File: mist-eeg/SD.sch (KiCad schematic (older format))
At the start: 24 parts, among them J4 Micro_SD_Card_Det, Q2 NMOS_DGS (3.3V), Q3 NMOS_DGS (3.3V), Q4 PMOS_DGS (3.3V @ 1A), SW3 SD_RST

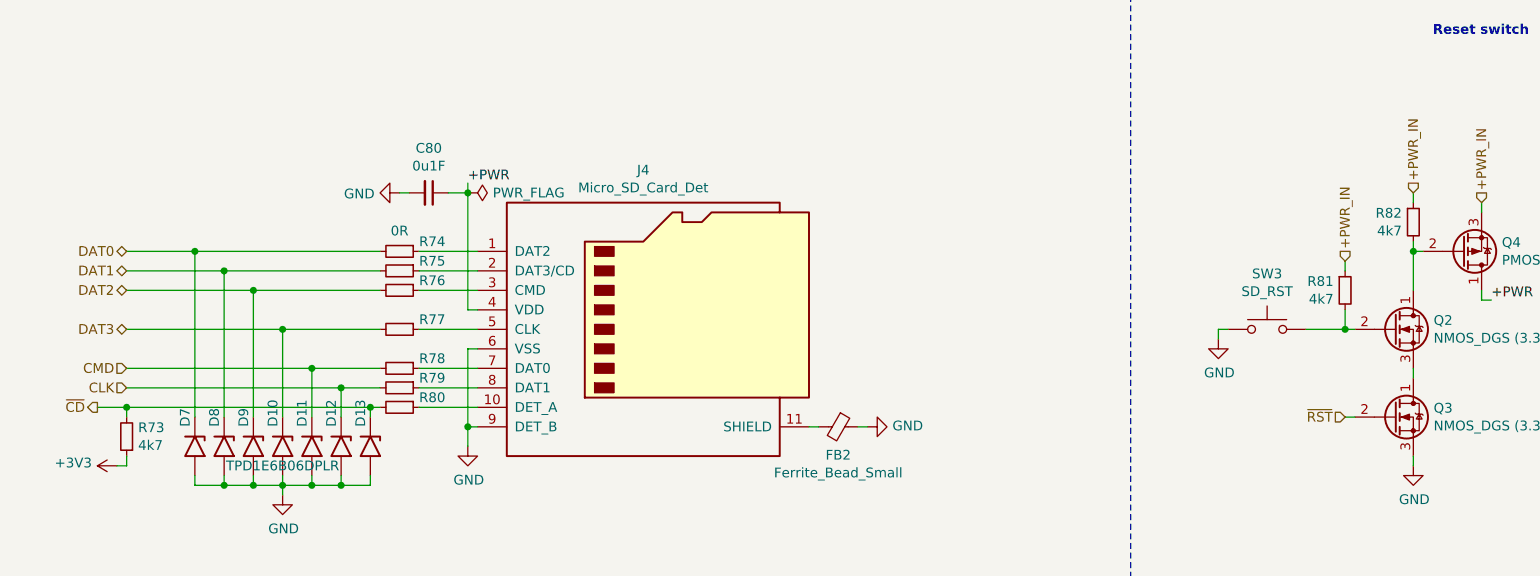
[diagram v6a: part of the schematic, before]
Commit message: Switch to POL switching regulator to accelerate production of the board
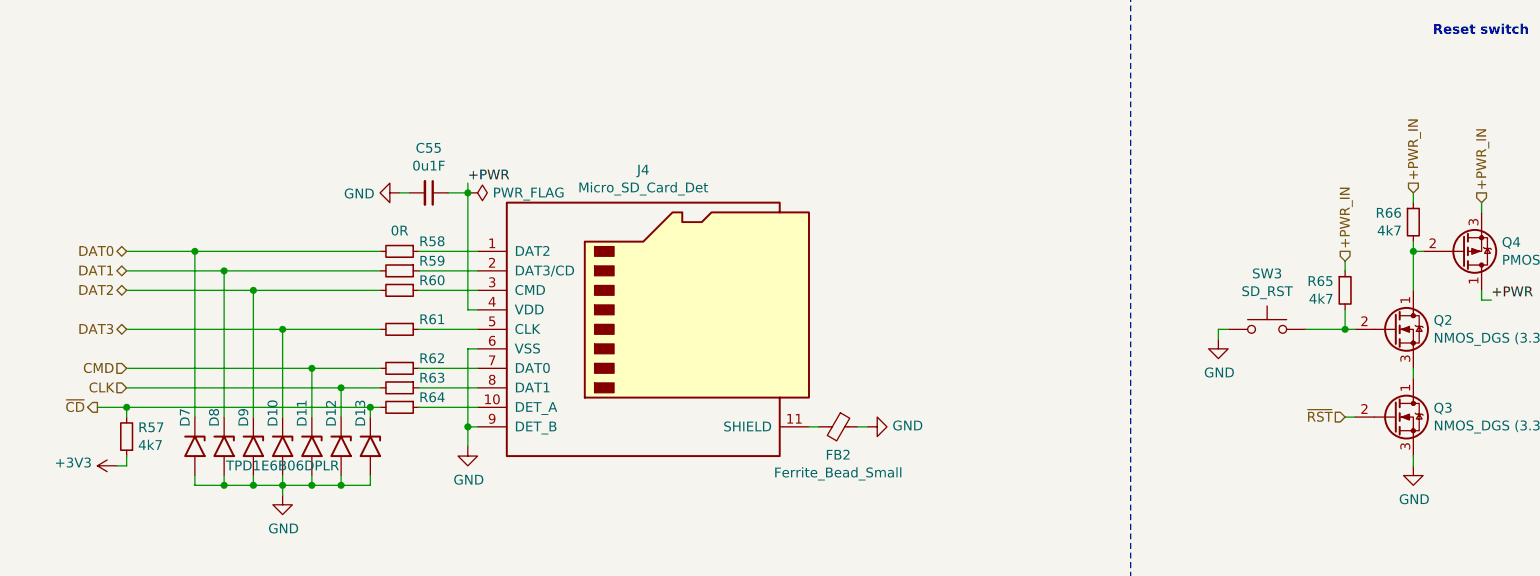
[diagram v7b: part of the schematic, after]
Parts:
- renumbered C80 to C55, R73 to R57, R74 to R58, R75 to R59, R76 to R60, R77 to R61, R78 to R62, R79 to R63, R80 to R64, R81 to R65, R82 to R66
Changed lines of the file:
@@
 $Descr USLetter 11000 8500
 encoding utf-8
-Sheet 10 11
+Sheet 7 8
 Title "Portiloop"
-Date "2021-08-03"
-Rev "1D"
+Date "2021-08-05"
+Rev "1E"
 Comp "MIST Lab"
 Comment1 "Designed by Xavier L'Heureux"
@@
 $EndComp
 $Comp
-L power:GND #PWR098
+L power:GND #PWR076
 U 1 1 60A29691
 P 3650 4500
-AR Path="/60A0E6BC/60A29691" Ref="#PWR098"  Part="1"
+AR Path="/60A0E6BC/60A29691" Ref="#PWR076"  Part="1"
 AR Path="/60A8612C/60A29691" Ref="#PWR?"  Part="1"
 AR Path="/60A7CCD6/60A29691" Ref="#PWR?"  Part="1"
-F 0 "#PWR098" H 3650 4250 50  0001 C CNN
+F 0 "#PWR076" H 3650 4250 50  0001 C CNN
 F 1 "GND" H 3655 4327 50  0000 C CNN
 F 2 "" H 3650 4500 50  0001 C CNN
@@
 	3700 3800 3650 3800
 $Comp
-L Device:R_Small R73
+L Device:R_Small R57
 U 1 1 60A2B32B
 P 1900 4450
-AR Path="/60A0E6BC/60A2B32B" Ref="R73"  Part="1"
+AR Path="/60A0E6BC/60A2B32B" Ref="R57"  Part="1"
 AR Path="/60A8612C/60A2B32B" Ref="R?"  Part="1"
 AR Path="/60A7CCD6/60A2B32B" Ref="R?"  Part="1"
-F 0 "R73" H 1841 4404 50  0000 R CNN
+F 0 "R57" H 1841 4404 50  0000 R CNN
 F 1 "4k7" H 1841 4495 50  0000 R CNN
 F 2 "Resistor_SMD:R_0201_0603Metric" H 1900 4450 50  0001 C CNN
@@
 +PWR
 $Comp
-L Device:R_Small R74
+L Device:R_Small R58
 U 1 1 60A76D6B
 P 3300 3500
-AR Path="/60A0E6BC/60A76D6B" Ref="R74"  Part="1"
+AR Path="/60A0E6BC/60A76D6B" Ref="R58"  Part="1"
 AR Path="/60A8612C/60A76D6B" Ref="R?"  Part="1"
 AR Path="/60A7CCD6/60A76D6B" Ref="R?"  Part="1"
-F 0 "R74" V 3250 3600 50  0000 L CNN
+F 0 "R58" V 3250 3600 50  0000 L CNN
 F 1 "0R" V 3195 3500 50  0000 C CNN
 F 2 "Resistor_SMD:R_0603_1608Metric" H 3300 3500 50  0001 C CNN
@@
 $EndComp
 $Comp
-L Device:R_Small R75
+L Device:R_Small R59
 U 1 1 60A76E23
 P 3300 3600
-AR Path="/60A0E6BC/60A76E23" Ref="R75"  Part="1"
+AR Path="/60A0E6BC/60A76E23" Ref="R59"  Part="1"
 AR Path="/60A8612C/60A76E23" Ref="R?"  Part="1"
 AR Path="/60A7CCD6/60A76E23" Ref="R?"  Part="1"
-F 0 "R75" V 3250 3700 50  0000 L CNN
+F 0 "R59" V 3250 3700 50  0000 L CNN
 F 1 "0R" V 3195 3600 50  0001 C CNN
 F 2 "Resistor_SMD:R_0603_1608Metric" H 3300 3600 50  0001 C CNN
@@
 $EndComp
 $Comp
-L Device:R_Small R78
+L Device:R_Small R62
 U 1 1 60A76FE9
 P 3300 4100
-AR Path="/60A0E6BC/60A76FE9" Ref="R78"  Part="1"
+AR Path="/60A0E6BC/60A76FE9" Ref="R62"  Part="1"
 AR Path="/60A8612C/60A76FE9" Ref="R?"  Part="1"
 AR Path="/60A7CCD6/60A76FE9" Ref="R?"  Part="1"
-F 0 "R78" V 3250 4200 50  0000 L CNN
+F 0 "R62" V 3250 4200 50  0000 L CNN
 F 1 "0R" V 3195 4100 50  0001 C CNN
 F 2 "Resistor_SMD:R_0603_1608Metric" H 3300 4100 50  0001 C CNN
@@
 $EndComp
 $Comp
-L Device:R_Small R79
+L Device:R_Small R63
 U 1 1 60A7708B
 P 3300 4200
-AR Path="/60A0E6BC/60A7708B" Ref="R79"  Part="1"
+AR Path="/60A0E6BC/60A7708B" Ref="R63"  Part="1"
 AR Path="/60A8612C/60A7708B" Ref="R?"  Part="1"
 AR Path="/60A7CCD6/60A7708B" Ref="R?"  Part="1"
-F 0 "R79" V 3250 4300 50  0000 L CNN
+F 0 "R63" V 3250 4300 50  0000 L CNN
 F 1 "0R" V 3195 4200 50  0001 C CNN
 F 2 "Resistor_SMD:R_0603_1608Metric" H 3300 4200 50  0001 C CNN
@@
 $EndComp
 $Comp
-L Device:R_Small R80
+L Device:R_Small R64
 U 1 1 60A7712D
 P 3300 4300
-AR Path="/60A0E6BC/60A7712D" Ref="R80"  Part="1"
+AR Path="/60A0E6BC/60A7712D" Ref="R64"  Part="1"
 AR Path="/60A8612C/60A7712D" Ref="R?"  Part="1"
 AR Path="/60A7CCD6/60A7712D" Ref="R?"  Part="1"
-F 0 "R80" V 3250 4400 50  0000 L CNN
+F 0 "R64" V 3250 4400 50  0000 L CNN
 F 1 "0R" V 3195 4300 50  0001 C CNN
 F 2 "Resistor_SMD:R_0603_1608Metric" H 3300 4300 50  0001 C CNN
@@
 	3400 3700 3700 3700
 $Comp
-L Device:C_Small C80
+L Device:C_Small C55
 U 1 1 60AB5AA5
 P 3450 3200
-AR Path="/60A0E6BC/60AB5AA5" Ref="C80"  Part="1"
+AR Path="/60A0E6BC/60AB5AA5" Ref="C55"  Part="1"
 AR Path="/60A7CCD6/60AB5AA5" Ref="C?"  Part="1"
-F 0 "C80" V 3221 3200 50  0000 C CNN
+F 0 "C55" V 3221 3200 50  0000 C CNN
 F 1 "0u1F" V 3312 3200 50  0000 C CNN
 F 2 "Capacitor_SMD:C_0201_0603Metric" H 3450 3200 50  0001 C CNN
@@
 	3400 4100 3700 4100
 $Comp
-L Device:R_Small R76
+L Device:R_Small R60
 U 1 1 60A76EC5
 P 3300 3700
-AR Path="/60A0E6BC/60A76EC5" Ref="R76"  Part="1"
+AR Path="/60A0E6BC/60A76EC5" Ref="R60"  Part="1"
 AR Path="/60A8612C/60A76EC5" Ref="R?"  Part="1"
 AR Path="/60A7CCD6/60A76EC5" Ref="R?"  Part="1"
-F 0 "R76" V 3250 3800 50  0000 L CNN
+F 0 "R60" V 3250 3800 50  0000 L CNN
 F 1 "0R" V 3195 3700 50  0001 C CNN
 F 2 "Resistor_SMD:R_0603_1608Metric" H 3300 3700 50  0001 C CNN
@@
 $EndComp
 $Comp
-L Device:R_Small R77
+L Device:R_Small R61
 U 1 1 60A76F57
 P 3300 3900
-AR Path="/60A0E6BC/60A76F57" Ref="R77"  Part="1"
+AR Path="/60A0E6BC/60A76F57" Ref="R61"  Part="1"
 AR Path="/60A8612C/60A76F57" Ref="R?"  Part="1"
 AR Path="/60A7CCD6/60A76F57" Ref="R?"  Part="1"
-F 0 "R77" V 3250 4000 50  0000 L CNN
+F 0 "R61" V 3250 4000 50  0000 L CNN
 F 1 "0R" V 3195 3900 50  0001 C CNN
 F 2 "Resistor_SMD:R_0603_1608Metric" H 3300 3900 50  0001 C CNN
@@
 	3400 3900 3700 3900
 $Comp
-L power:+3V3 #PWR095
+L power:+3V3 #PWR073
 U 1 1 6116A372
 P 1850 4600
-F 0 "#PWR095" H 1850 4450 50  0001 C CNN
+F 0 "#PWR073" H 1850 4450 50  0001 C CNN
 F 1 "+3V3" V 1865 4728 50  0000 L CNN
 F 2 "" H 1850 4600 50  0001 C CNN
@@
 	2250 3500 3200 3500
 $Comp
-L power:GND #PWR096
+L power:GND #PWR074
 U 1 1 611F8FF2
 P 2700 4750
-F 0 "#PWR096" H 2700 4500 50  0001 C CNN
+F 0 "#PWR074" H 2700 4500 50  0001 C CNN
 F 1 "GND" H 2705 4577 50  0000 C CNN
 F 2 "" H 2700 4750 50  0001 C CNN
@@
 	8150 4350 8200 4350
 $Comp
-L power:GND #PWR0101
+L power:GND #PWR079
 U 1 1 6124838F
 P 8500 4600
-F 0 "#PWR0101" H 8500 4350 50  0001 C CNN
+F 0 "#PWR079" H 8500 4350 50  0001 C CNN
 F 1 "GND" H 8505 4427 50  0000 C CNN
 F 2 "" H 8500 4600 50  0001 C CNN
@@
 +PWR_IN
 $Comp
-L Device:R_Small R82
+L Device:R_Small R66
 U 1 1 6125B0BC
 P 8500 3350
-F 0 "R82" H 8441 3396 50  0000 R CNN
+F 0 "R66" H 8441 3396 50  0000 R CNN
 F 1 "4k7" H 8441 3305 50  0000 R CNN
 F 2 "Resistor_SMD:R_0201_0603Metric" H 8500 3350 50  0001 C CNN
@@
 $EndComp
 $Comp
-L power:GND #PWR097
+L power:GND #PWR075
 U 1 1 6130D5F8
 P 3300 3200
-F 0 "#PWR097" H 3300 2950 50  0001 C CNN
+F 0 "#PWR075" H 3300 2950 50  0001 C CNN
 F 1 "GND" V 3305 3072 50  0000 R CNN
 F 2 "" H 3300 3200 50  0001 C CNN
@@
 P 5700 4400
 AR Path="/610A6E66" Ref="#PWR?"  Part="1"
-AR Path="/60A0E6BC/610A6E66" Ref="#PWR099"  Part="1"
-F 0 "#PWR099" H 5700 4150 50  0001 C CNN
+AR Path="/60A0E6BC/610A6E66" Ref="#PWR077"  Part="1"
+F 0 "#PWR077" H 5700 4150 50  0001 C CNN
 F 1 "GND" V 5705 4272 50  0000 R CNN
 F 2 "" H 5700 4400 50  0001 C CNN
@@
 +PWR_IN
 $Comp
-L Device:R_Small R81
+L Device:R_Small R65
 U 1 1 6108C1B2
 P 8150 3700
-F 0 "R81" H 8091 3746 50  0000 R CNN
+F 0 "R65" H 8091 3746 50  0000 R CNN
 F 1 "4k7" H 8091 3655 50  0000 R CNN
 F 2 "Resistor_SMD:R_0201_0603Metric" H 8150 3700 50  0001 C CNN
@@
 	8150 3900 8200 3900
 $Comp
-L power:GND #PWR0100
+L power:GND #PWR078
 U 1 1 61092F2A
 P 7500 3950
-F 0 "#PWR0100" H 7500 3700 50  0001 C CNN
+F 0 "#PWR078" H 7500 3700 50  0001 C CNN
 F 1 "GND" H 7505 3777 50  0000 C CNN
 F 2 "" H 7500 3950 50  0001 C CNN
